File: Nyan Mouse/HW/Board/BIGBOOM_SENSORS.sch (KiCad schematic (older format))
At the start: 19 parts

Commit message: Made changes to board 20% done still. :/
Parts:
- added R? (x6): 1.8k, symbol R
- added RE1, RE2, RE3, RE4, RE5, RE6: OPTO_NPN, symbol OPTO_NPN
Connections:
- net +3.3VP: now reaches R?.1
- net +3.3VP: now also R?.1, R?.1, R?.1, R?.1, R?.1
- new net +3.3VA: R?.1, R?.1, R?.1, R?.1, R?.1, R?.1
- new net AGND: RE1.1 (E), RE2.1 (E), RE3.1 (E), RE4.1 (E), RE5.1 (E), RE6.1 (E)
- new net re1: R?.2, RE1.3 (C)
- new net re2: R?.2, RE2.3 (C)
- new net re3: R?.2, RE3.3 (C)
- new net re4: R?.2, RE4.3 (C)
- new net re5: R?.2, RE5.3 (C)
- new net re6: R?.2, RE6.3 (C)
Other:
- moved on the sheet: E1, E2, E3, E4, E5, E6, Q?, R?, U?

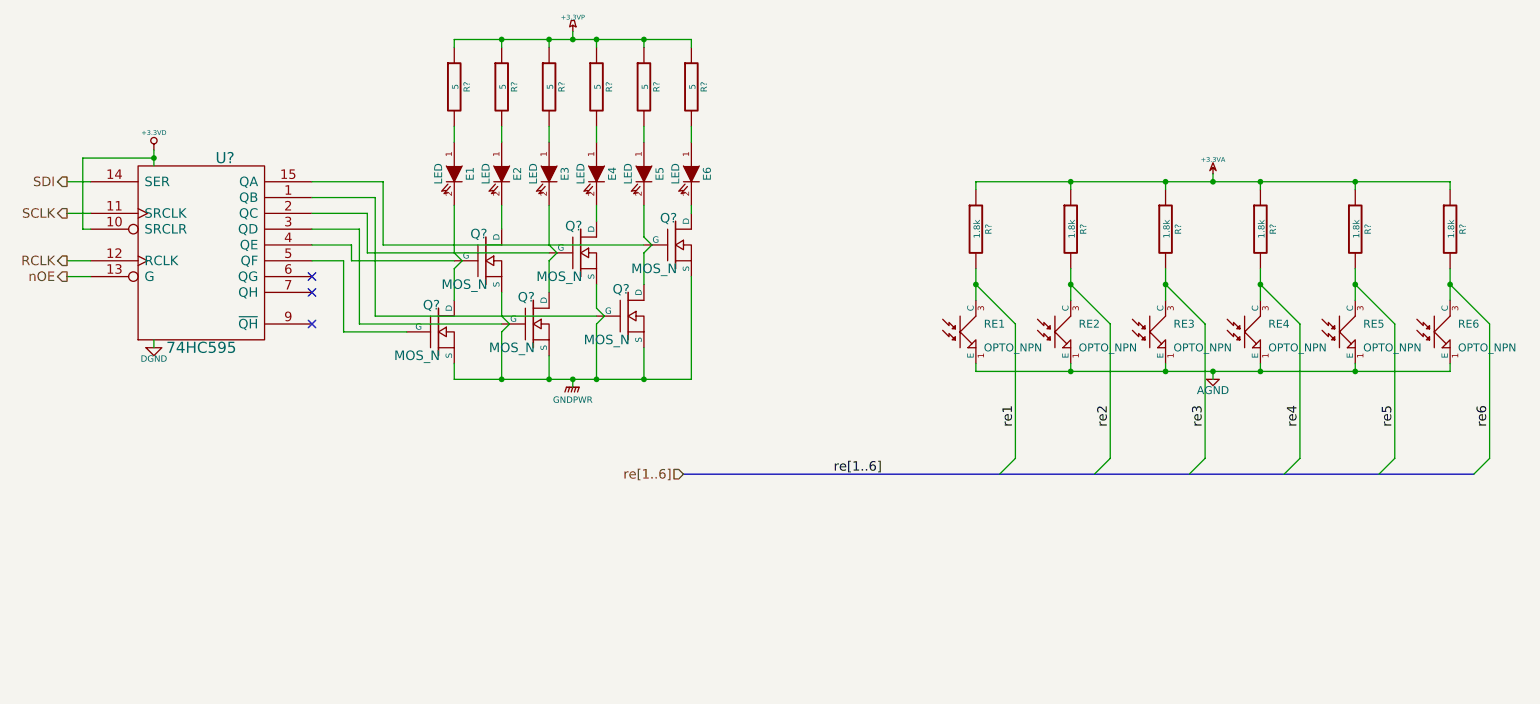
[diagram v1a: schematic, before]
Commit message: Changed DRV8837, Almost completed main board. ERC almost successful.
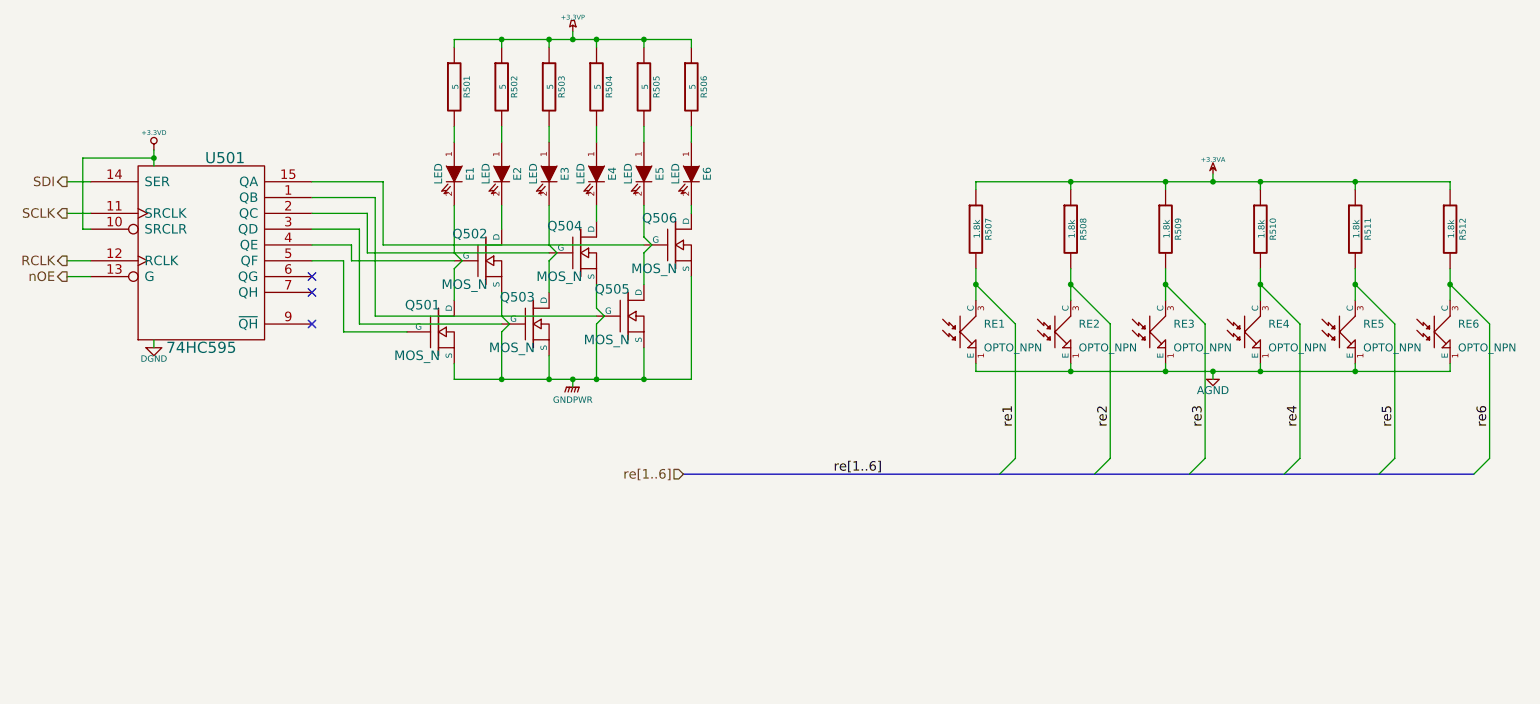
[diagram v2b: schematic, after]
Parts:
- gave numbers to parts that had none: 19
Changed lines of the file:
@@
 encoding utf-8
 Sheet 5 5
-Title ""
-Date ""
-Rev ""
-Comp ""
+Title "Nyan Mouse"
+Date "23 Apr 2014"
+Rev "Alpha"
+Comp "IEEE UCR"
 Comment1 ""
 Comment2 ""
@@
 $EndComp
 $Comp
-L MOS_N Q?
+L MOS_N Q506
 U 1 1 5357BDA1
 P 4700 2050
-F 0 "Q?" H 4710 2220 60  0000 R CNN
+F 0 "Q506" H 4710 2220 60  0000 R CNN
 F 1 "MOS_N" H 4710 1900 60  0000 R CNN
 F 2 "" H 4700 2050 60  0000 C CNN
@@
 $EndComp
 $Comp
-L MOS_N Q?
+L MOS_N Q504
 U 1 1 5357BDB5
 P 4100 2100
-F 0 "Q?" H 4110 2270 60  0000 R CNN
+F 0 "Q504" H 4110 2270 60  0000 R CNN
 F 1 "MOS_N" H 4110 1950 60  0000 R CNN
 F 2 "" H 4100 2100 60  0000 C CNN
@@
 $EndComp
 $Comp
-L MOS_N Q?
+L MOS_N Q502
 U 1 1 5357BDC7
 P 3500 2150
-F 0 "Q?" H 3510 2320 60  0000 R CNN
+F 0 "Q502" H 3510 2320 60  0000 R CNN
 F 1 "MOS_N" H 3510 2000 60  0000 R CNN
 F 2 "" H 3500 2150 60  0000 C CNN
@@
 $EndComp
 $Comp
-L MOS_N Q?
+L MOS_N Q505
 U 1 1 5357BDD7
 P 4400 2500
-F 0 "Q?" H 4410 2670 60  0000 R CNN
+F 0 "Q505" H 4410 2670 60  0000 R CNN
 F 1 "MOS_N" H 4410 2350 60  0000 R CNN
 F 2 "" H 4400 2500 60  0000 C CNN
@@
 $EndComp
 $Comp
-L MOS_N Q?
+L MOS_N Q503
 U 1 1 5357BDE7
 P 3800 2550
-F 0 "Q?" H 3810 2720 60  0000 R CNN
+F 0 "Q503" H 3810 2720 60  0000 R CNN
 F 1 "MOS_N" H 3810 2400 60  0000 R CNN
 F 2 "" H 3800 2550 60  0000 C CNN
@@
 $EndComp
 $Comp
-L MOS_N Q?
+L MOS_N Q501
 U 1 1 5357BDF7
 P 3200 2600
-F 0 "Q?" H 3210 2770 60  0000 R CNN
+F 0 "Q501" H 3210 2770 60  0000 R CNN
 F 1 "MOS_N" H 3210 2450 60  0000 R CNN
 F 2 "" H 3200 2600 60  0000 C CNN
@@
 $EndComp
 $Comp
-L GNDPWR #PWR?
+L GNDPWR #PWR056
 U 1 1 5357BFB1
 P 4050 2950
-F 0 "#PWR?" H 4050 3000 40  0001 C CNN
+F 0 "#PWR056" H 4050 3000 40  0001 C CNN
 F 1 "GNDPWR" H 4050 2870 40  0000 C CNN
 F 2 "" H 4050 2950 60  0000 C CNN
@@
 $EndComp
 $Comp
-L 74HC595 U?
+L 74HC595 U501
 U 1 1 5357C0F7
 P 1700 2100
-F 0 "U?" H 1850 2700 70  0000 C CNN
+F 0 "U501" H 1850 2700 70  0000 C CNN
 F 1 "74HC595" H 1700 1500 70  0000 C CNN
 F 2 "" H 1700 2100 60  0000 C CNN
@@
 SCLK
 $Comp
-L DGND #PWR?
+L DGND #PWR057
 U 1 1 5357DEDF
 P 1400 2700
-F 0 "#PWR?" H 1400 2700 40  0001 C CNN
+F 0 "#PWR057" H 1400 2700 40  0001 C CNN
 F 1 "DGND" H 1400 2630 40  0000 C CNN
 F 2 "" H 1400 2700 60  0000 C CNN
@@
 $EndComp
 $Comp
-L +3.3VD #PWR?
+L +3.3VD #PWR058
 U 1 1 5357DEF3
 P 1400 1450
-F 0 "#PWR?" H 1400 1410 30  0001 C CNN
+F 0 "#PWR058" H 1400 1410 30  0001 C CNN
 F 1 "+3.3VD" H 1400 1560 30  0000 C CNN
 F 2 "" H 1400 1450 60  0000 C CNN
@@
 SDI
 $Comp
-L R R?
+L R R501
 U 1 1 5357EB59
 P 3300 1050
-F 0 "R?" V 3380 1050 40  0000 C CNN
+F 0 "R501" V 3380 1050 40  0000 C CNN
 F 1 "5" V 3307 1051 40  0000 C CNN
 F 2 "" V 3230 1050 30  0000 C CNN
@@
 $EndComp
 $Comp
-L R R?
+L R R502
 U 1 1 5357EBB2
 P 3600 1050
-F 0 "R?" V 3680 1050 40  0000 C CNN
+F 0 "R502" V 3680 1050 40  0000 C CNN
 F 1 "5" V 3607 1051 40  0000 C CNN
 F 2 "" V 3530 1050 30  0000 C CNN
@@
 $EndComp
 $Comp
-L R R?
+L R R503
 U 1 1 5357EBB9
 P 3900 1050
-F 0 "R?" V 3980 1050 40  0000 C CNN
+F 0 "R503" V 3980 1050 40  0000 C CNN
 F 1 "5" V 3907 1051 40  0000 C CNN
 F 2 "" V 3830 1050 30  0000 C CNN
@@
 $EndComp
 $Comp
-L R R?
+L R R504
 U 1 1 5357EBC0
 P 4200 1050
-F 0 "R?" V 4280 1050 40  0000 C CNN
+F 0 "R504" V 4280 1050 40  0000 C CNN
 F 1 "5" V 4207 1051 40  0000 C CNN
 F 2 "" V 4130 1050 30  0000 C CNN
@@
 $EndComp
 $Comp
-L R R?
+L R R505
 U 1 1 5357EBC7
 P 4500 1050
-F 0 "R?" V 4580 1050 40  0000 C CNN
+F 0 "R505" V 4580 1050 40  0000 C CNN
 F 1 "5" V 4507 1051 40  0000 C CNN
 F 2 "" V 4430 1050 30  0000 C CNN
@@
 $EndComp
 $Comp
-L R R?
+L R R506
 U 1 1 5357EBCE
 P 4800 1050
-F 0 "R?" V 4880 1050 40  0000 C CNN
+F 0 "R506" V 4880 1050 40  0000 C CNN
 F 1 "5" V 4807 1051 40  0000 C CNN
 F 2 "" V 4730 1050 30  0000 C CNN
@@
 $EndComp
 $Comp
-L +3.3VP #PWR?
+L +3.3VP #PWR059
 U 1 1 5358178D
 P 4050 700
-F 0 "#PWR?" H 4100 730 20  0001 C CNN
+F 0 "#PWR059" H 4100 730 20  0001 C CNN
 F 1 "+3.3VP" H 4050 790 30  0000 C CNN
 F 2 "" H 4050 700 60  0000 C CNN
@@
 $EndComp
 $Comp
-L +3.3VA #PWR?
+L +3.3VA #PWR060
 U 1 1 5358765E
 P 8100 1600
-F 0 "#PWR?" H 8100 1720 20  0001 C CNN
+F 0 "#PWR060" H 8100 1720 20  0001 C CNN
 F 1 "+3.3VA" H 8100 1690 30  0000 C CNN
 F 2 "" H 8100 1600 60  0000 C CNN
@@
 $EndComp
 $Comp
-L AGND #PWR?
+L AGND #PWR061
 U 1 1 535876B6
 P 8100 2900
-F 0 "#PWR?" H 8100 2900 40  0001 C CNN
+F 0 "#PWR061" H 8100 2900 40  0001 C CNN
 F 1 "AGND" H 8100 2830 50  0000 C CNN
 F 2 "" H 8100 2900 60  0000 C CNN
@@
 $EndComp
 $Comp
-L R R?
+L R R512
 U 1 1 535879AA
 P 9600 1950
-F 0 "R?" V 9680 1950 40  0000 C CNN
+F 0 "R512" V 9680 1950 40  0000 C CNN
 F 1 "1.8k" V 9607 1951 40  0000 C CNN
 F 2 "" V 9530 1950 30  0000 C CNN
@@
 $EndComp
 $Comp
-L R R?
+L R R511
 U 1 1 535879BC
 P 9000 1950
-F 0 "R?" V 9080 1950 40  0000 C CNN
+F 0 "R511" V 9080 1950 40  0000 C CNN
 F 1 "1.8k" V 9007 1951 40  0000 C CNN
 F 2 "" V 8930 1950 30  0000 C CNN
@@
 $EndComp
 $Comp
-L R R?
+L R R510
 U 1 1 535879CC
 P 8400 1950
-F 0 "R?" V 8480 1950 40  0000 C CNN
+F 0 "R510" V 8480 1950 40  0000 C CNN
 F 1 "1.8k" V 8407 1951 40  0000 C CNN
 F 2 "" V 8330 1950 30  0000 C CNN
@@
 $EndComp
 $Comp
-L R R?
+L R R509
 U 1 1 535879DC
 P 7800 1950
-F 0 "R?" V 7880 1950 40  0000 C CNN
+F 0 "R509" V 7880 1950 40  0000 C CNN
 F 1 "1.8k" V 7807 1951 40  0000 C CNN
 F 2 "" V 7730 1950 30  0000 C CNN
@@
 $EndComp
 $Comp
-L R R?
+L R R508
 U 1 1 535879EC
 P 7200 1950
-F 0 "R?" V 7280 1950 40  0000 C CNN
+F 0 "R508" V 7280 1950 40  0000 C CNN
 F 1 "1.8k" V 7207 1951 40  0000 C CNN
 F 2 "" V 7130 1950 30  0000 C CNN
@@
 $EndComp
 $Comp
-L R R?
+L R R507
 U 1 1 535879FC
 P 6600 1950
-F 0 "R?" V 6680 1950 40  0000 C CNN
+F 0 "R507" V 6680 1950 40  0000 C CNN
 F 1 "1.8k" V 6607 1951 40  0000 C CNN
 F 2 "" V 6530 1950 30  0000 C CNN
